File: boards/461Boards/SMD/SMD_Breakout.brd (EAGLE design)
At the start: 25.4 x 25.4 mm, 7 parts, among them U1 ATTINY461A-SUATTINY461A-QFN

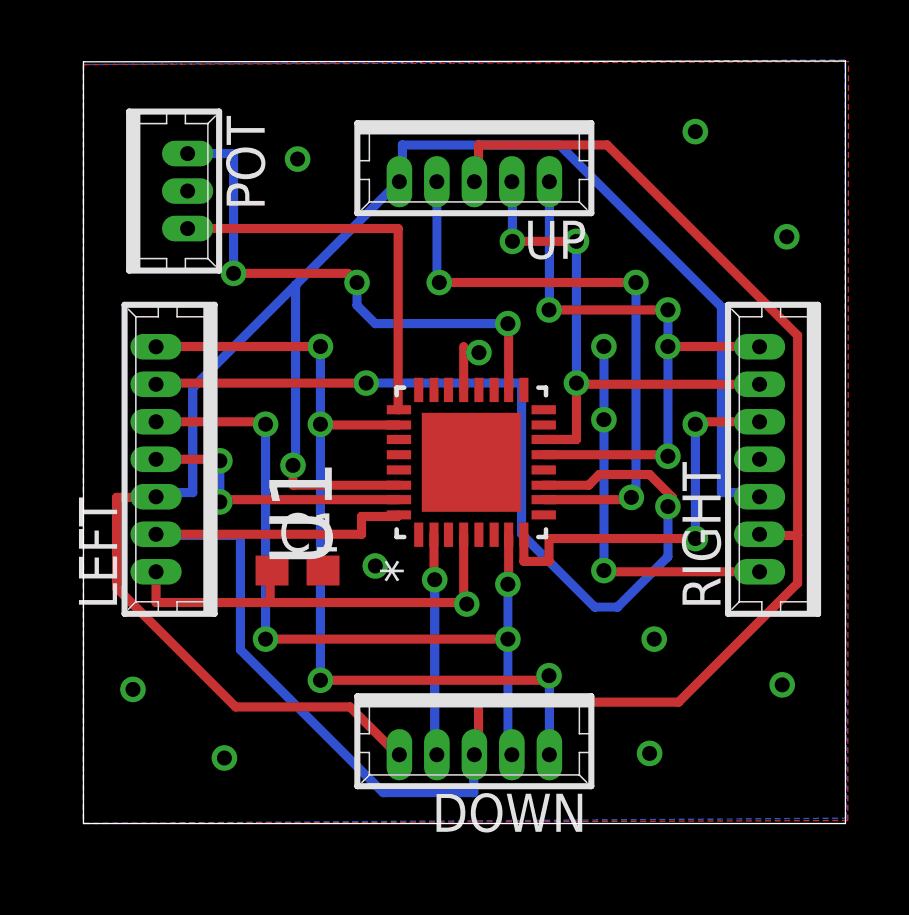
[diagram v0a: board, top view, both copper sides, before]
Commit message: SMD Breakout with layout complete ( all pins to the frame board with global reset). Board progress issue updated with pinouts and layout guide for design review.
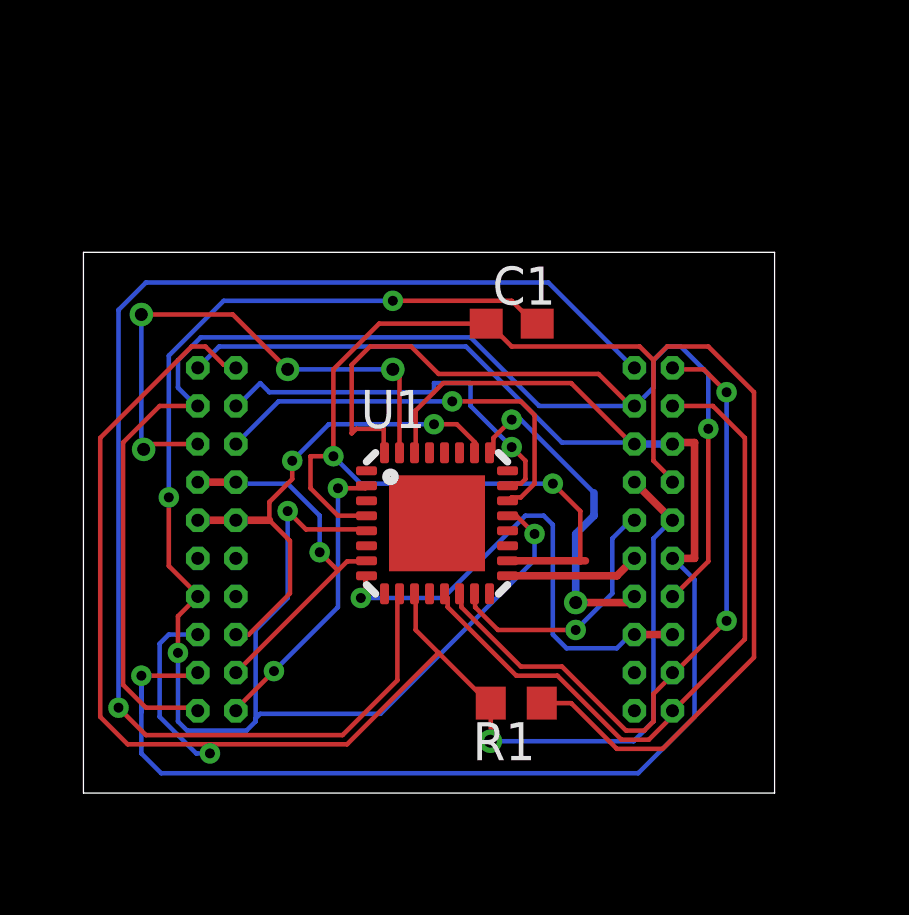
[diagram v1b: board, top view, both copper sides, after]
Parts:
- removed DOWN, UP: 53047-05, con-molex:53047-05
- removed LEFT, RIGHT: 53047-07, con-molex:53047-07
- removed POT: 53047-03, con-molex:53047-03
- added IN, OUT: 2X10_0.05_HEADERCUSTOM1, Custom:2X10_CUSTOM
- added R1: (no value), rcl:R0603
- U1: value ATTINY461A-SUATTINY461A-QFN -> ATTINY461A-SUMLF-32-TH; device Atmel_By_element14_Batch_1-00:QFN50P500X500X100-32N -> Atmel_By_element14_Batch_1-00:MLF32-TH
- moved C1 10.9 mm to (14.3, 16.7)
- moved U1 2.33 mm to (11.8, 10.0), turned to 0 degrees
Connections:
- removed net CLK_IN: DOWN.4, LEFT.3, U1.7
- removed net CLK_OUT: RIGHT.2, U1.14, UP.4
- removed net DOWN: DOWN.2, U1.2
- removed net N$1: LEFT.2, U1.11
- removed net N$2: POT.1, U1.25
- removed net UP: U1.10, UP.2
- new net ABOVE: OUT.PIN1, U1.10
- new net BELOW: IN.PIN20, U1.2
- new net ELED: OUT.PIN9, U1.15
- new net M_CLK: OUT.PIN18, OUT.PIN2, U1.14
- new net PA2: IN.PIN4, U1.23
- new net PA3: IN.PIN6, U1.22
- new net POT: OUT.PIN13, U1.25
- new net RESET: IN.PIN15, IN.PIN2, OUT.PIN10, OUT.PIN7, R1.2, U1.11
- new net SLED: OUT.PIN11, U1.17
- new net S_CLK: IN.PIN18, IN.PIN7, IN.PIN8, U1.7
- net GND: now also IN.PIN13; no longer POT.2, RIGHT.7
- net LEFT: now also IN.PIN5; no longer LEFT.4
- net MDO: now also OUT.PIN20, OUT.PIN4; no longer RIGHT.1, UP.5
- net RIGHT: now also OUT.PIN15, OUT.PIN16; no longer RIGHT.3
- net SCL: now also IN.PIN19, IN.PIN3, OUT.PIN14, OUT.PIN3; no longer DOWN.3, LEFT.6, RIGHT.6, UP.3
- net SDA: now also IN.PIN1, IN.PIN17, OUT.PIN12, OUT.PIN5, OUT.PIN6; no longer DOWN.1, LEFT.5, RIGHT.5, UP.1
- net SDI: now also IN.PIN10, IN.PIN16, IN.PIN9; no longer DOWN.5, LEFT.1
- net VDD: now also OUT.PIN8, R1.1; no longer LEFT.7, POT.3
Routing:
- net RESET: track 0.00 -> 55.6 mm, vias 0 -> 2
- net ABOVE: track 0.00 -> 45.3 mm, vias 0 -> 1
- net GND: track 14.1 -> 52.9 mm, vias 13 -> 5
- net N$1: track 30.6 -> 0.00 mm, vias 2 -> 0
- net CLK_IN: track 26.5 -> 0.00 mm, vias 4 -> 0
- net VDD: track 32.8 -> 58.3 mm, vias 3 -> 2
- net M_CLK: track 0.00 -> 22.8 mm, vias 0 -> 2
- net UP: track 20.3 -> 0.00 mm, vias 3 -> 0
- net CLK_OUT: track 17.9 -> 0.00 mm, vias 3 -> 0
- net PA3: track 0.00 -> 14.2 mm, vias 0 -> 1
- net PA2: track 0.00 -> 13.2 mm, vias 0 -> 1
- net N$2: track 13.1 -> 0.00 mm
- net SDI: track 29.7 -> 17.0 mm, vias 4 -> 2
- net S_CLK: track 0.00 -> 12.5 mm, vias 0 -> 1
- net POT: track 0.00 -> 11.2 mm, vias 0 -> 2
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- removed copper zone on layer 1, net GND
- removed copper zone on layer 16, net GND
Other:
- board size 25.4 x 25.4 mm -> 23 x 18 mm
